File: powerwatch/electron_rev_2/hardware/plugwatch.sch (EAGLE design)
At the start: 110 parts, among them J1 DM3AT-SF-PEJM5, J2 TC2030-JLINK-NL, SW4 SIP32510, U1 BGA725L6-ALT, U10 SIP32510, U11 SIP32510, U12 SIP32510, U2 SAFFB1G56KB0F0A, U3 ISL29035, U4 MAX-M8, U5 MAX740XESA, U6 MPU-9250, U7 NRF51822QF, U8 OPA322AIDBVT, U9 SIP32510, X1 ABS05-32.768KHZ-9-T, X2 16MHz

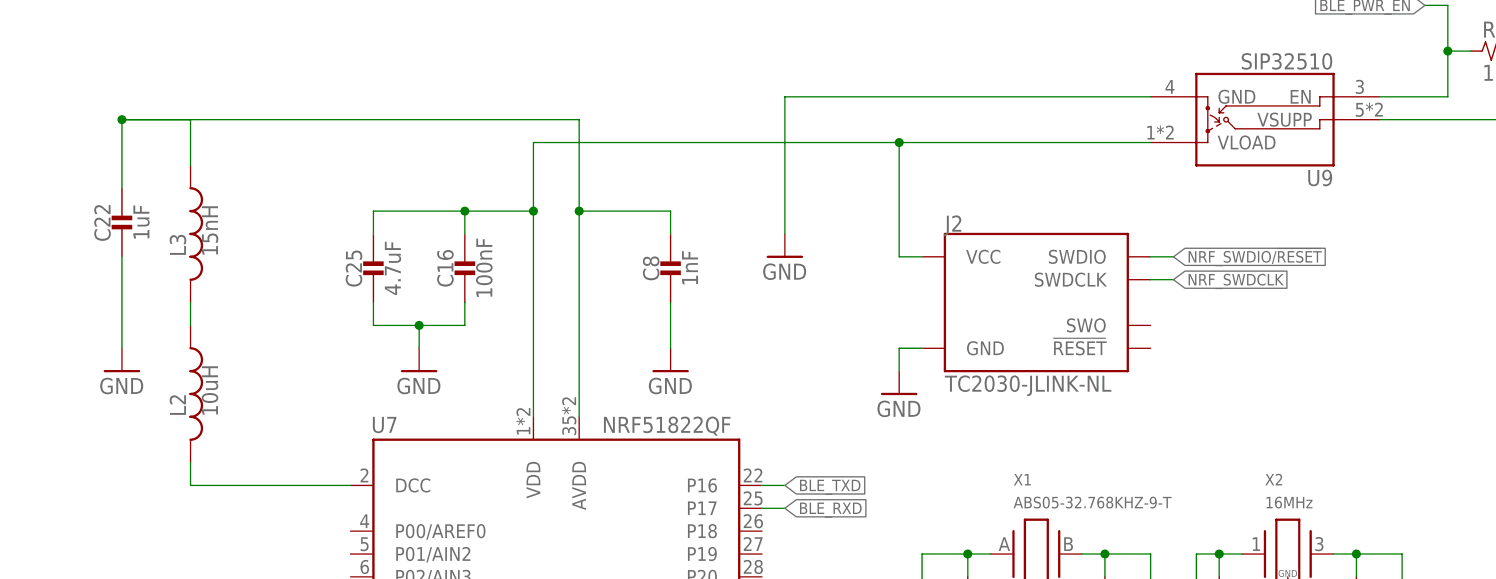
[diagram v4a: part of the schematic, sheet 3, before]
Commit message: fixed up silk, renumber chips
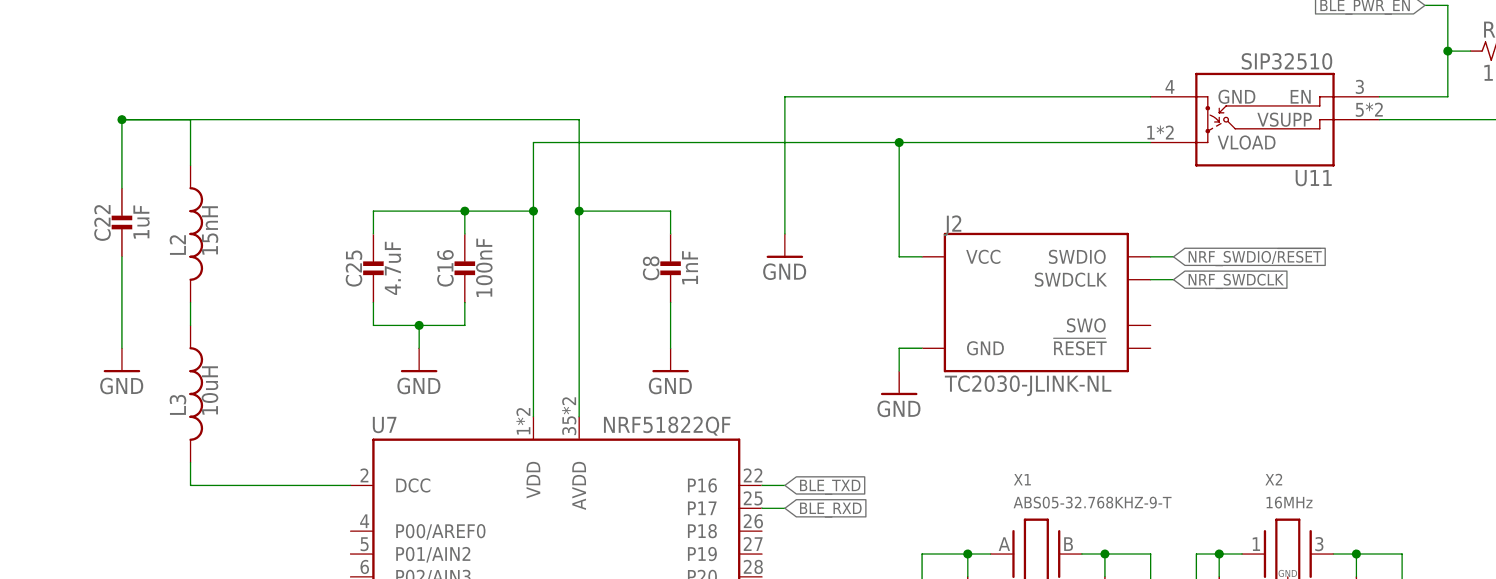
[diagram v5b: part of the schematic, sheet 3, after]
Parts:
- removed SW4: SIP32510, chips:SIP32510
- added U13: SIP32510, chips:SIP32510
- L2: value 10uH -> 15nH; device passives:INDUCTOR0603 -> passives:INDUCTOR0402; DIGIKEY 490-4025-1-ND -> 587-1521-1-ND
- L3: value 15nH -> 10uH; device passives:INDUCTOR0402 -> passives:INDUCTOR0603; DIGIKEY 587-1521-1-ND -> 490-4025-1-ND
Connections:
- net AUDIO_PWR_EN: now also U13.EN; no longer U11.EN
- net AVDD1: now also L2.1; no longer L3.1
- net BLE_PWR_EN: now also U11.EN; no longer U9.EN
- net DCC1: now also L3.2; no longer L2.2
- net GND: now also U13.GND; no longer SW4.GND
- net GPS_PWR_EN: now also U10.EN; no longer U12.EN
- net GPS_VCC: now also U10.VLOAD; no longer U12.VLOAD
- net N$14: now also U9.VLOAD; no longer SW4.VLOAD
- net N$15: now also L2.2, L3.1; no longer L2.1, L3.2
- net N$18: now also U12.VLOAD; no longer U10.VLOAD
- net SD_ENABLE_POWER: now also U12.EN; no longer U10.EN
- net VCC: now also U13.VSUPP; no longer SW4.VSUPP
- net VCC_A_MIC: now also U13.VLOAD; no longer U11.VLOAD
- net VCC_BLE: now also U11.VLOAD; no longer U9.VLOAD
- net WIFI_PWR_EN: now also U9.EN; no longer SW4.EN
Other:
- moved on the sheet: L2, L3
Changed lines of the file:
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@@
 <part name="GND9" library="supply1" library_urn="urn:adsk.eagle:library:371" deviceset="GND" device=""/>
 <part name="B1" library="chips" deviceset="BAL-NRF01D3" device=""/>
-<part name="L3" library="passives" deviceset="INDUCTOR" device="0402" value="15nH">
+<part name="L2" library="passives" deviceset="INDUCTOR" device="0402" value="15nH">
 <attribute name="DIGIKEY" value="587-1521-1-ND"/>
 </part>
@@
 <attribute name="DIGIKEY" value="RMCF0402FT1K00CT-ND"/>
 </part>
-<part name="L2" library="passives" deviceset="INDUCTOR" device="0603" value="10uH">
+<part name="L3" library="passives" deviceset="INDUCTOR" device="0603" value="10uH">
 <attribute name="DIGIKEY" value="490-4025-1-ND"/>
 </part>
@@
 <part name="GND34" library="supply1" library_urn="urn:adsk.eagle:library:371" deviceset="GND" device=""/>
 <part name="P+15" library="supply1" library_urn="urn:adsk.eagle:library:371" deviceset="VCC" device=""/>
-<part name="SW4" library="chips" deviceset="SIP32510" device=""/>
+<part name="U9" library="chips" deviceset="SIP32510" device=""/>
 <part name="P+16" library="supply1" library_urn="urn:adsk.eagle:library:371" deviceset="VCC" device=""/>
 <part name="GND35" library="supply1" library_urn="urn:adsk.eagle:library:371" deviceset="GND" device=""/>
@@
 <part name="TP24" library="headers" deviceset="TEST_POINT_0.040IN" device=""/>
 <part name="TP25" library="headers" deviceset="TEST_POINT_0.040IN" device=""/>
-<part name="U12" library="chips" deviceset="SIP32510" device=""/>
-<part name="U9" library="chips" deviceset="SIP32510" device=""/>
 <part name="U10" library="chips" deviceset="SIP32510" device=""/>
 <part name="U11" library="chips" deviceset="SIP32510" device=""/>
+<part name="U12" library="chips" deviceset="SIP32510" device=""/>
+<part name="U13" library="chips" deviceset="SIP32510" device=""/>
 </parts>
 <sheets>
@@
 <instance part="TP24" gate="G$1" x="215.9" y="71.12" rot="R180"/>
 <instance part="TP25" gate="G$1" x="215.9" y="68.58" rot="R180"/>
-<instance part="U10" gate="G$1" x="45.72" y="48.26"/>
+<instance part="U12" gate="G$1" x="45.72" y="48.26"/>
 </instances>
 <busses>
@@
 <wire x1="66.04" y1="53.34" x2="66.04" y2="33.02" width="0.1524" layer="91"/>
 <junction x="66.04" y="33.02"/>
-<pinref part="U10" gate="G$1" pin="GND"/>
+<pinref part="U12" gate="G$1" pin="GND"/>
 </segment>
 <segment>
@@
 <junction x="35.56" y="43.18"/>
 <pinref part="R17" gate="G$1" pin="1"/>
-<pinref part="U10" gate="G$1" pin="EN"/>
+<pinref part="U12" gate="G$1" pin="EN"/>
 </segment>
 </net>
@@
 <wire x1="66.04" y1="68.58" x2="71.12" y2="68.58" width="0.1524" layer="91"/>
 <wire x1="66.04" y1="58.42" x2="66.04" y2="68.58" width="0.1524" layer="91"/>
-<pinref part="U10" gate="G$1" pin="VLOAD"/>
+<pinref part="U12" gate="G$1" pin="VLOAD"/>
 </segment>
 </net>
@@
 <pinref part="P+2" gate="VCC" pin="VCC"/>
 <pinref part="R17" gate="G$1" pin="2"/>
-<pinref part="U10" gate="G$1" pin="VSUPP"/>
+<pinref part="U12" gate="G$1" pin="VSUPP"/>
 </segment>
 <segment>
@@
 </instance>
 <instance part="P+15" gate="VCC" x="119.38" y="78.74"/>
-<instance part="SW4" gate="G$1" x="99.06" y="71.12" rot="R180"/>
+<instance part="U9" gate="G$1" x="99.06" y="71.12" rot="R180"/>
 <instance part="GND35" gate="1" x="53.34" y="50.8"/>
 <instance part="R19" gate="G$1" x="114.3" y="71.12">
 <attribute name="DIGIKEY" x="114.3" y="71.12" size="1.27" layer="96" font="vector" display="off"/>
 </instance>
-<instance part="U12" gate="G$1" x="154.94" y="172.72" rot="R180"/>
+<instance part="U10" gate="G$1" x="154.94" y="172.72" rot="R180"/>
 </instances>
 <busses>
@@
 <wire x1="109.22" y1="175.26" x2="109.22" y2="170.18" width="0.1524" layer="91"/>
 <junction x="109.22" y="170.18"/>
-<pinref part="U12" gate="G$1" pin="GND"/>
+<pinref part="U10" gate="G$1" pin="GND"/>
 </segment>
 <segment>
@@
 </segment>
 <segment>
-<pinref part="SW4" gate="G$1" pin="GND"/>
+<pinref part="U9" gate="G$1" pin="GND"/>
 <wire x1="78.74" y1="66.04" x2="53.34" y2="66.04" width="0.1524" layer="91"/>
 <wire x1="53.34" y1="66.04" x2="53.34" y2="53.34" width="0.1524" layer="91"/>
@@
 <wire x1="160.02" y1="167.64" x2="162.56" y2="167.64" width="0.1524" layer="91"/>
 <junction x="162.56" y="172.72"/>
-<pinref part="U12" gate="G$1" pin="EN"/>
+<pinref part="U10" gate="G$1" pin="EN"/>
 </segment>
 </net>
@@
 <wire x1="139.7" y1="154.94" x2="137.16" y2="154.94" width="0.1524" layer="91"/>
 <junction x="137.16" y="154.94"/>
-<pinref part="U12" gate="G$1" pin="VLOAD"/>
+<pinref part="U10" gate="G$1" pin="VLOAD"/>
 <junction x="134.62" y="162.56"/>
 </segment>
@@
 <wire x1="172.72" y1="172.72" x2="175.26" y2="172.72" width="0.1524" layer="91"/>
 <junction x="175.26" y="172.72"/>
-<pinref part="U12" gate="G$1" pin="VSUPP"/>
+<pinref part="U10" gate="G$1" pin="VSUPP"/>
 </segment>
 <segment>
@@
 <wire x1="116.84" y1="71.12" x2="119.38" y2="71.12" width="0.1524" layer="91"/>
 <junction x="119.38" y="71.12"/>
-<pinref part="SW4" gate="G$1" pin="VSUPP"/>
+<pinref part="U9" gate="G$1" pin="VSUPP"/>
 <wire x1="119.38" y1="63.5" x2="104.14" y2="63.5" width="0.1524" layer="91"/>
 <pinref part="R19" gate="G$1" pin="2"/>
@@
 <wire x1="88.9" y1="53.34" x2="73.66" y2="53.34" width="0.1524" layer="91"/>
 <junction x="73.66" y="53.34"/>
-<pinref part="SW4" gate="G$1" pin="VLOAD"/>
+<pinref part="U9" gate="G$1" pin="VLOAD"/>
 <wire x1="78.74" y1="60.96" x2="73.66" y2="60.96" width="0.1524" layer="91"/>
 <wire x1="73.66" y1="60.96" x2="73.66" y2="53.34" width="0.1524" layer="91"/>
@@
 <net name="WIFI_PWR_EN" class="0">
 <segment>
-<pinref part="SW4" gate="G$1" pin="EN"/>
+<pinref part="U9" gate="G$1" pin="EN"/>
 <wire x1="106.68" y1="66.04" x2="104.14" y2="66.04" width="0.1524" layer="91"/>
 <wire x1="106.68" y1="66.04" x2="106.68" y2="71.12" width="0.1524" layer="91"/>
@@
 <instance part="GND9" gate="1" x="165.1" y="40.64"/>
 <instance part="B1" gate="G$1" x="147.32" y="76.2"/>
-<instance part="L3" gate="G$1" x="35.56" y="157.48">
+<instance part="L2" gate="G$1" x="35.56" y="157.48">
 <attribute name="DIGIKEY" x="35.56" y="157.48" size="1.778" layer="96" display="off"/>
 </instance>
@@
 <attribute name="DIGIKEY" x="33.02" y="109.22" size="1.27" layer="96" rot="R270" display="off"/>
 </instance>
-<instance part="L2" gate="G$1" x="35.56" y="139.7">
+<instance part="L3" gate="G$1" x="35.56" y="139.7">
 <attribute name="DIGIKEY" x="35.56" y="139.7" size="1.778" layer="96" display="off"/>
 </instance>
@@
 </instance>
 <instance part="GND36" gate="1" x="101.6" y="154.94"/>
-<instance part="U9" gate="G$1" x="162.56" y="177.8" rot="R180"/>
+<instance part="U11" gate="G$1" x="162.56" y="177.8" rot="R180"/>
 </instances>
 <busses>
@@
 <wire x1="101.6" y1="172.72" x2="101.6" y2="157.48" width="0.1524" layer="91"/>
 <pinref part="GND36" gate="1" pin="GND"/>
-<pinref part="U9" gate="G$1" pin="GND"/>
+<pinref part="U11" gate="G$1" pin="GND"/>
 </segment>
 </net>
@@
 <pinref part="C8" gate="G$1" pin="1"/>
 <wire x1="88.9" y1="157.48" x2="88.9" y2="160.02" width="0.1524" layer="91"/>
-<pinref part="L3" gate="G$1" pin="1"/>
+<pinref part="L2" gate="G$1" pin="1"/>
 <wire x1="35.56" y1="165.1" x2="35.56" y2="170.18" width="0.1524" layer="91"/>
 <pinref part="U7" gate="G$1" pin="AVDD"/>
@@
 <wire x1="53.34" y1="129.54" x2="35.56" y2="129.54" width="0.1524" layer="91"/>
 <wire x1="35.56" y1="129.54" x2="35.56" y2="132.08" width="0.1524" layer="91"/>
+<pinref part="L3" gate="G$1" pin="2"/>
+</segment>
+</net>
+<net name="N$15" class="0">
+<segment>
 <pinref part="L2" gate="G$1" pin="2"/>
-</segment>
-</net>
-<net name="N$15" class="0">
-<segment>
-<pinref part="L3" gate="G$1" pin="2"/>
 <wire x1="35.56" y1="147.32" x2="35.56" y2="149.86" width="0.1524" layer="91"/>
-<pinref part="L2" gate="G$1" pin="1"/>
+<pinref part="L3" gate="G$1" pin="1"/>
 </segment>
 </net>
@@
 <wire x1="187.96" y1="170.18" x2="167.64" y2="170.18" width="0.1524" layer="91"/>
 <pinref part="R20" gate="G$1" pin="2"/>
-<pinref part="U9" gate="G$1" pin="VSUPP"/>
+<pinref part="U11" gate="G$1" pin="VSUPP"/>
 </segment>
 </net>
@@
 <wire x1="73.66" y1="167.64" x2="73.66" y2="160.02" width="0.1524" layer="91"/>
 <junction x="114.3" y="167.64"/>
-<pinref part="U9" gate="G$1" pin="VLOAD"/>
+<pinref part="U11" gate="G$1" pin="VLOAD"/>
 </segment>
 <segment>
@@
 <junction x="175.26" y="177.8"/>
 <pinref part="R20" gate="G$1" pin="1"/>
-<pinref part="U9" gate="G$1" pin="EN"/>
+<pinref part="U11" gate="G$1" pin="EN"/>
 </segment>
 </net>
@@
 <attribute name="DIGIKEY" x="180.34" y="175.26" size="1.27" layer="96" font="vector" display="off"/>
 </instance>
-<instance part="U11" gate="G$1" x="162.56" y="175.26" rot="R180"/>
+<instance part="U13" gate="G$1" x="162.56" y="175.26" rot="R180"/>
 </instances>
 <busses>
@@
 <wire x1="121.92" y1="170.18" x2="121.92" y2="160.02" width="0.1524" layer="91"/>
 <pinref part="GND34" gate="1" pin="GND"/>
-<pinref part="U11" gate="G$1" pin="GND"/>
+<pinref part="U13" gate="G$1" pin="GND"/>
 </segment>
 </net>
@@
 <wire x1="185.42" y1="167.64" x2="167.64" y2="167.64" width="0.1524" layer="91"/>
 <pinref part="R21" gate="G$1" pin="2"/>
-<pinref part="U11" gate="G$1" pin="VSUPP"/>
+<pinref part="U13" gate="G$1" pin="VSUPP"/>
 </segment>
 </net>
@@
 <junction x="142.24" y="154.94"/>
 <wire x1="142.24" y1="165.1" x2="142.24" y2="154.94" width="0.1524" layer="91"/>
-<pinref part="U11" gate="G$1" pin="VLOAD"/>
+<pinref part="U13" gate="G$1" pin="VLOAD"/>
 </segment>
 </net>
@@
 <junction x="172.72" y="175.26"/>
 <pinref part="R21" gate="G$1" pin="1"/>
-<pinref part="U11" gate="G$1" pin="EN"/>
-</segment>
-</net>
+<pinref part="U13" gate="G$1" pin="EN"/>
+</segment>
+</net>
